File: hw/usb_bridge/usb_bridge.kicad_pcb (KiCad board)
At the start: 2 copper layers, 51 x 31 mm, 55 parts, among them J1 USB_C_Receptacle_USB2.0_14P, J2 DE9, J3 SWD, J4 BOOT, U1 CH340E, U2 MAX485E, U3 CH334R, U4 74LVC2G04, U5 MCP1754S-3302xCB, U6 TJA1051T-3, U7 STM32G0B1CBT, Y1 HCI XC53G2-12.000-F20LJDT, Y2 HCI XC53G2-8.000-F12NJHP

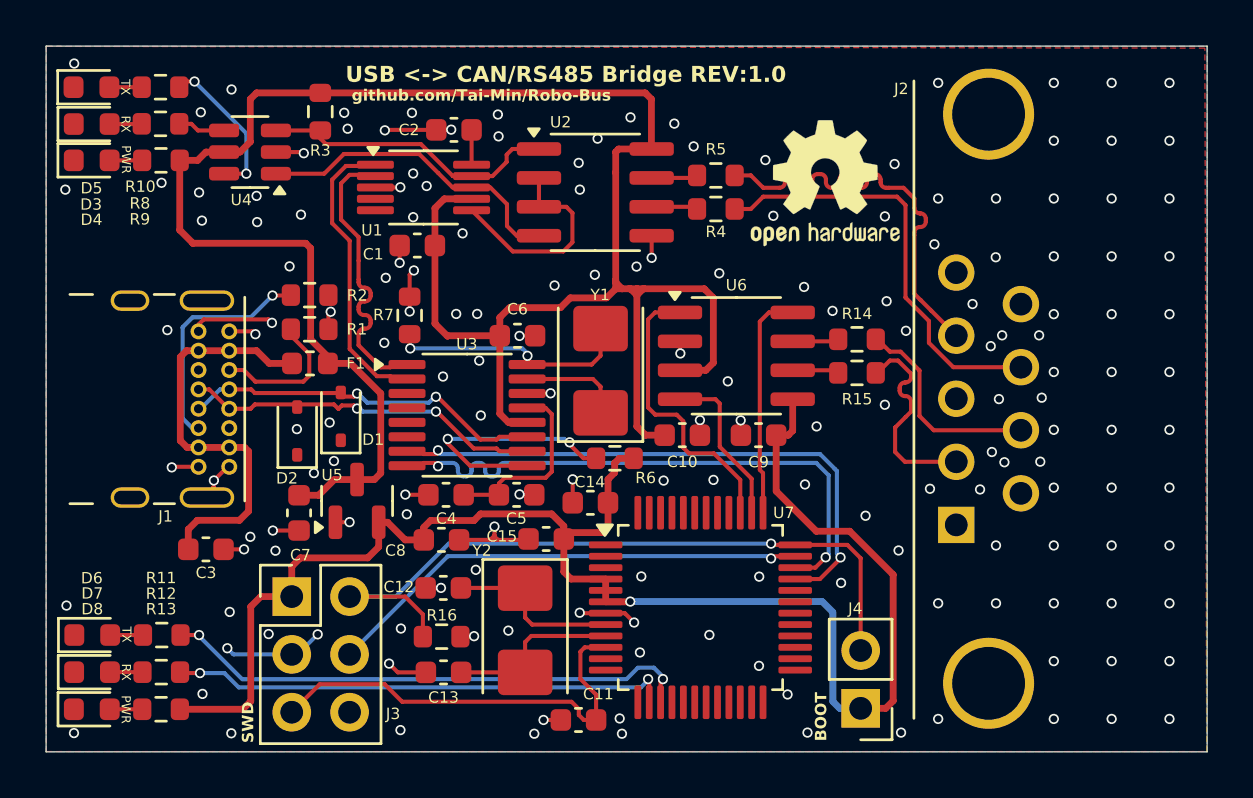
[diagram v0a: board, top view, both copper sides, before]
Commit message: Add jumpers and test points, add QR code
Signed-off-by: Mateusz Pająk <22417805+Tai-Min@users.noreply.github.com>
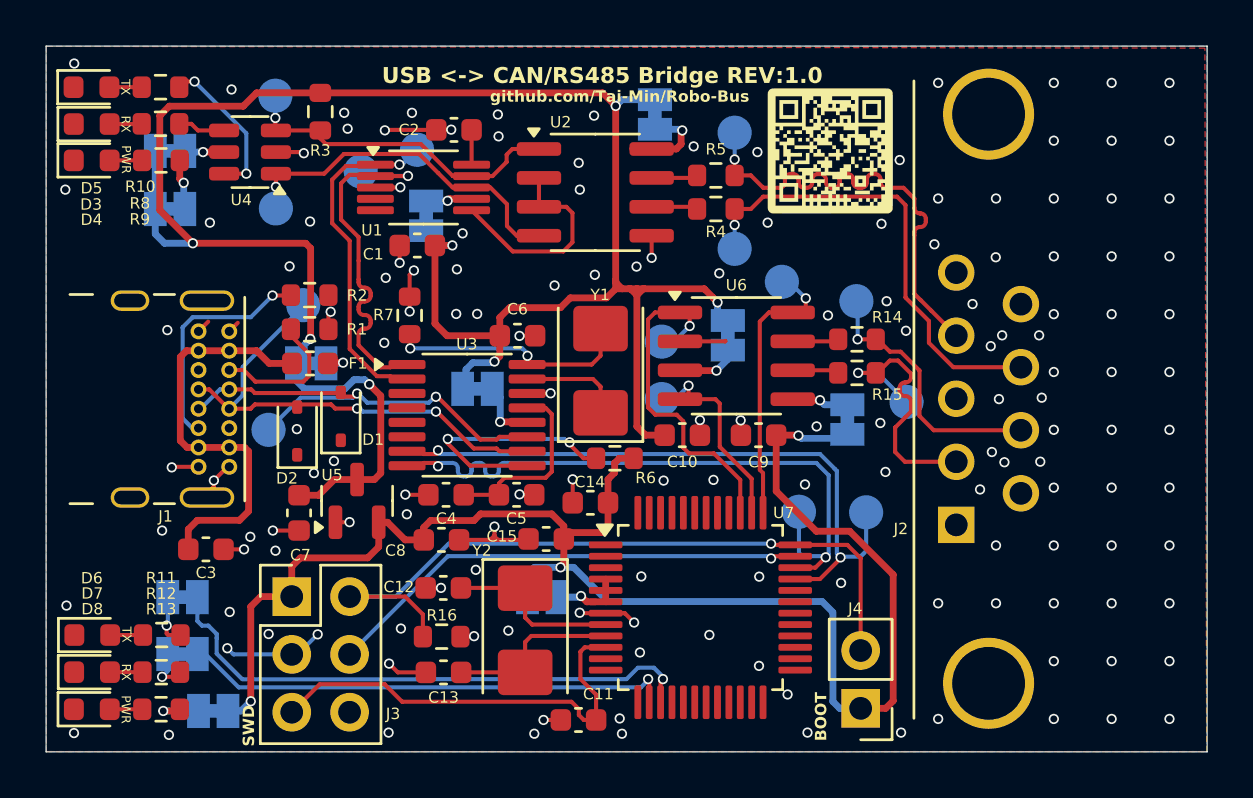
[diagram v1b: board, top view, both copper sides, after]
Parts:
- added G***: LOGO, symbols:robo-bus-qr-small, F.Cu at (160.9, 91.7)
- added JP1: Diode cutoff, Jumper:SolderJumper-2_P1.3mm_Bridged_Pad1.0x1.5mm, B.Cu at (131.9, 93.7)
- added JP10: Diode cutoff, Jumper:SolderJumper-2_P1.3mm_Bridged_Pad1.0x1.5mm, B.Cu at (132.4, 110.8)
- added JP11: Amp TP, Jumper:SolderJumper-2_P1.3mm_Bridged_Pad1.0x1.5mm, B.Cu at (148.2, 110.8)
- added JP12: Amp TP, Jumper:SolderJumper-2_P1.3mm_Bridged_Pad1.0x1.5mm, B.Cu at (161.7, 103.0)
- added JP2: Diode cutoff, Jumper:SolderJumper-2_P1.3mm_Bridged_Pad1.0x1.5mm, B.Cu at (133.8, 115.8)
- added JP3: Diode cutoff, Jumper:SolderJumper-2_P1.3mm_Bridged_Pad1.0x1.5mm, B.Cu at (131.9, 91.2)
- added JP4: Amp TP, Jumper:SolderJumper-2_P1.3mm_Bridged_Pad1.0x1.5mm, B.Cu at (138.1, 100.5)
- added JP5: Amp TP, Jumper:SolderJumper-2_P1.3mm_Bridged_Pad1.0x1.5mm, B.Cu at (145.4, 101.6)
- added JP6: Amp TP, Jumper:SolderJumper-2_P1.3mm_Bridged_Pad1.0x1.5mm, B.Cu at (156.4, 99.2)
- added JP7: Amp TP, Jumper:SolderJumper-2_P1.3mm_Bridged_Pad1.0x1.5mm, B.Cu at (153.2, 89.5)
- added JP8: Amp TP, Jumper:SolderJumper-2_P1.3mm_Bridged_Pad1.0x1.5mm, B.Cu at (143.2, 94.0)
- added JP9: Diode cutoff, Jumper:SolderJumper-2_P1.3mm_Bridged_Pad1.0x1.5mm, B.Cu at (132.4, 113.2)
- added TP1: TestPoint, TestPoint:TestPoint_Pad_D1.5mm, B.Cu at (158.8, 96.9)
- added TP10: TestPoint, TestPoint:TestPoint_Pad_D1.5mm, B.Cu at (137.8, 97.9)
- added TP11: TestPoint, TestPoint:TestPoint_Pad_D1.5mm, B.Cu at (136.2, 103.4)
- added TP12: TestPoint, TestPoint:TestPoint_Pad_D1.5mm, B.Cu at (156.7, 95.5)
- added TP13: TestPoint, TestPoint:TestPoint_Pad_D1.5mm, B.Cu at (156.7, 90.3)
- added TP14: TestPoint, TestPoint:TestPoint_Pad_D1.5mm, B.Cu at (164.2, 102.2)
- added TP15: TestPoint, TestPoint:TestPoint_Pad_D1.5mm, B.Cu at (162.1, 97.8)
- added TP2: TestPoint, TestPoint:TestPoint_Pad_D1.5mm, B.Cu at (153.5, 102.0)
- added TP3: TestPoint, TestPoint:TestPoint_Pad_D1.5mm, B.Cu at (153.5, 99.5)
- added TP4: TestPoint, TestPoint:TestPoint_Pad_D1.5mm, B.Cu at (136.6, 93.7)
- added TP5: TestPoint, TestPoint:TestPoint_Pad_D1.5mm, B.Cu at (136.5, 88.7)
- added TP6: TestPoint, TestPoint:TestPoint_Pad_D1.5mm, B.Cu at (140.3, 92.0)
- added TP7: TestPoint, TestPoint:TestPoint_Pad_D1.5mm, B.Cu at (142.8, 91.1)
- added TP8: TestPoint, TestPoint:TestPoint_Pad_D1.5mm, B.Cu at (162.5, 107.0)
- added TP9: TestPoint, TestPoint:TestPoint_Pad_D1.5mm, B.Cu at (159.5, 107.0)
- REF**: moved to B.Cu
- moved REF** 43.8 mm to (172.9, 110.4), turned to -90 degrees
- moved REF** 15.2 mm to (173.8, 100.4), turned to -90 degrees
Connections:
- F1 pad 2: +5V -> Net-(JP4-A)
- R10 pad 2: +5V -> Net-(JP1-A)
- R11 pad 2: /mcu/LED_TX -> Net-(JP10-A)
- R12 pad 2: /mcu/LED_RX -> Net-(JP9-A)
- R13 pad 2: +3.3V -> Net-(JP2-A)
- U1 pad 7: +5V -> Net-(JP8-A)
- U2 pad 8: +5V -> Net-(JP7-A)
- U3 pad 12: +5V -> Net-(JP5-A)
- U4 pad 5: +5V -> Net-(JP3-A)
- U6 pad 3: +5V -> Net-(JP6-A)
- U6 pad 5: +3.3V -> Net-(JP12-A)
- U7 pad 4: +3.3V -> Net-(JP11-A)
- U7 pad 5: +3.3V -> Net-(JP11-A)
- U7 pad 6: +3.3V -> Net-(JP11-A)
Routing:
- net /D-: track 15.9 -> 21.7 mm
- net /D+: track 16.1 -> 20.6 mm
- net Net-(JP7-A): track 0.00 -> 4.07 mm, vias 0 -> 1
- net /D_RS-: track 12.9 -> 16.5 mm, vias 0 -> 1
- net /CAN-: track 9.16 -> 12.6 mm, vias 0 -> 1
- net /D_CAN+: track 25.5 -> 28.6 mm
- net /D_CAN-: track 25.6 -> 28.5 mm
- net Net-(JP11-A): track 0.00 -> 2.81 mm, vias 0 -> 1
- net Net-(JP5-A): track 0.00 -> 2.79 mm, vias 0 -> 1
- net Net-(JP6-A): track 0.00 -> 2.71 mm, vias 0 -> 1
- net Net-(JP12-A): track 0.00 -> 2.50 mm, vias 0 -> 1
- net /CAN+: track 9.20 -> 11.7 mm, vias 0 -> 1
- net /mcu/CAN_TX: track 12.9 -> 15.4 mm, vias 0 -> 1
- net /mcu/CAN_S: track 10.1 -> 12.5 mm, vias 0 -> 1
- net /mcu/CAN_RX: track 7.20 -> 9.52 mm, vias 0 -> 1
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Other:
- board text added: "3V3 LED"
- board text added: "5V LED"
- board text added: "CAN AMP TP"
- board text added: "CAN IO AMP TP"
- board text added: "CAN RX"
- board text added: "CAN RX LED"
- board text added: "CAN S"
- board text added: "CAN TX"
- board text added: "CAN TX LED"
- board text added: "CAN+"
- board text added: "CAN-"
- board text added: "D+"
- board text added: "D+ CAN"
- board text added: "D+ RS485"
- board text added: "D-"
- board text added: "D- CAN"
- board text added: "D- RS485"
- board text added: "HUB AMP TP"
- board text added: "PWR AMP TP"
- board text added: "RS485 AMP TP"
- board text added: "RS485 LEDS"
- board text added: "RS485 RX"
- board text added: "RS485 TX"
- board text added: "RS485+"
- board text added: "RS485-"
- board text added: "STM AMP TP"
- board text added: "UART AMP TP"

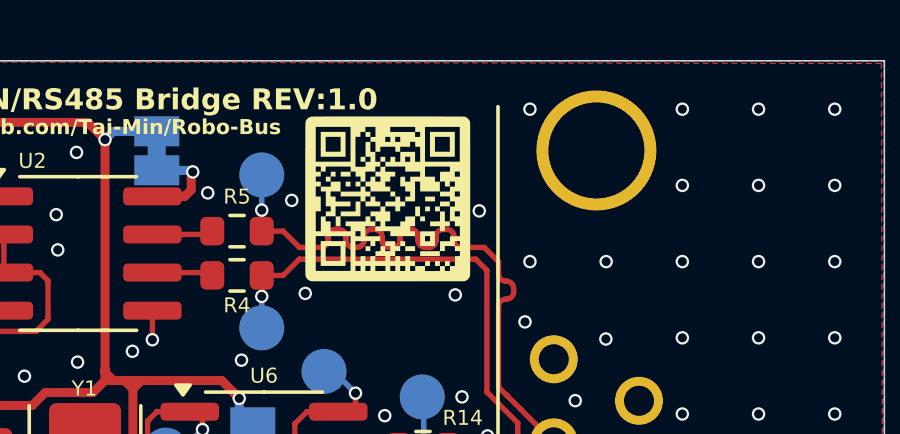
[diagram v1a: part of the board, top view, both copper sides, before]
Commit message: Add gnd test point
Signed-off-by: Mateusz Pająk <22417805+Tai-Min@users.noreply.github.com>
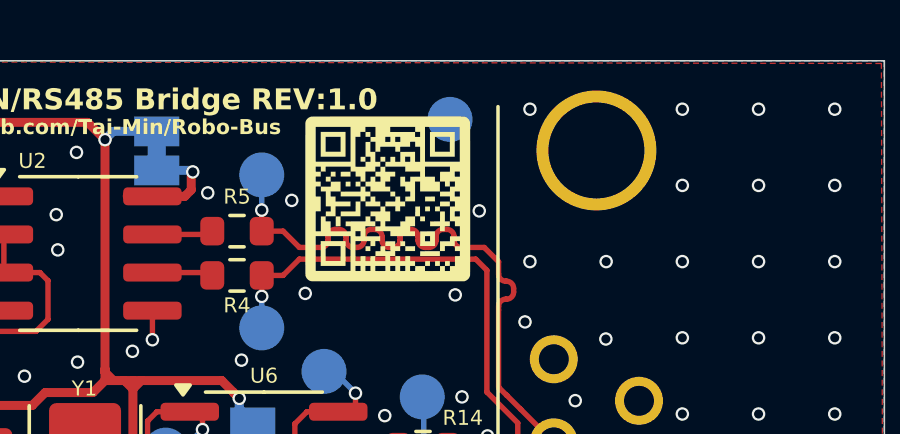
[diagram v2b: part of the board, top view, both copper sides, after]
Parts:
- added TP16: TestPoint, TestPoint:TestPoint_Pad_D1.5mm, B.Cu at (163.0, 88.5)
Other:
- board text added: "GND"
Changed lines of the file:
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@@
+	(footprint "TestPoint:TestPoint_Pad_D1.5mm"
+		(layer "B.Cu")
+		(at 162.975 88.5 180)
+		(descr "SMD pad as test Point, diameter 1.5mm")
+		(tags "test point SMD pad")
+		(property "Reference" "TP16"
+			(at 0 1.648 0)
+			(layer "B.SilkS")
+			(hide yes)
+			(effects
+				(font
+					(size 1 1)
+					(thickness 0.15)
+				)
+				(justify mirror)
+			)
+		)
+		(property "Value" "TestPoint"
+			(at 0 -1.75 0)
+			(layer "B.Fab")
+			(effects
+				(font
+					(size 1 1)
+					(thickness 0.15)
+				)
+				(justify mirror)
+			)
+		)
+		(property "Datasheet" "~"
+			(at 0 0 0)
+			(unlocked yes)
+			(layer "B.Fab")
+			(hide yes)
+			(effects
+				(font
+					(size 1.27 1.27)
+					(thickness 0.15)
+				)
+				(justify mirror)
+			)
+		)
+		(property "Description" "test point"
+			(at 0 0 0)
+			(unlocked yes)
+			(layer "B.Fab")
+			(hide yes)
+			(effects
+				(font
+					(size 1.27 1.27)
+					(thickness 0.15)
+				)
+				(justify mirror)
+			)
+		)
+		(property ki_fp_filters "Pin* Test*")
+		(sheetname "/")
+		(sheetfile "usb_bridge.kicad_sch")
+		(attr exclude_from_pos_files)
+		(fp_circle
+			(center 0 0)
+			(end 0 -0.95)
+			(stroke
+				(width 0.12)
+				(type solid)
+			)
+			(fill no)
+			(layer "B.SilkS")
+		)
+		(fp_circle
+			(center 0 0)
+			(end 1.25 0)
+			(stroke
+				(width 0.05)
+				(type solid)
+			)
+			(fill no)
+			(layer "B.CrtYd")
+		)
+		(fp_text user "${REFERENCE}"
+			(at 0 1.65 0)
+			(layer "B.Fab")
+			(effects
+				(font
+					(size 1 1)
+					(thickness 0.15)
+				)
+				(justify mirror)
+			)
+		)
+		(pad "1" smd circle
+			(at 0 0 180)
+			(size 1.5 1.5)
+			(layers "B.Cu" "B.Mask")
+			(net 1 "GND")
+			(pinfunction "1")
+			(pintype "passive")
+		)
+		(embedded_fonts no)
+	)
 	(footprint "TestPoint:TestPoint_Pad_D1.5mm"
 		(layer "B.Cu")
@@
 		(layer "B.SilkS")
 		(effects
+			(font
+				(size 0.5 0.5)
+				(thickness 0.125)
+				(bold yes)
+			)
+			(justify left bottom mirror)
+		)
+	)
+	(gr_text "GND"
+		(at 163.8 90.325 0)
+		(layer "B.SilkS")
+		(effects

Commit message: Change versioning
Signed-off-by: Mateusz Pająk <22417805+Tai-Min@users.noreply.github.com>
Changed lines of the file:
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@@
 	(paper "A4")
 	(title_block
-		(title "USB <-> CAN/RS485 Bridge")
+		(title "${TITLE}")
 		(date "2025-11-24")
-		(rev "1.0")
+		(rev "${REVISION}")
 	)
 	(layers
@@
 		)
 	)
-	(property "REVISION" "1.0")
+	(property "REVISION" "1.0.0d")
 	(property "TITLE" "USB <-> CAN / RS485 ADAPTER")
 	(net 0 "")
@@
 	)
 	(gr_text "${TITLE} REV:${REVISION}"
-		(at 141.2 88.25 0)
+		(at 163.7792 88.2904 0)
 		(layer "F.SilkS")
 		(effects
@@
 				(bold yes)
 			)
-			(justify left bottom)
+			(justify right bottom)
 		)
 	)

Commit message: Cleanup
Signed-off-by: Mateusz Pająk <22417805+Tai-Min@users.noreply.github.com>
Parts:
- removed JP1, JP10, JP2, JP3, JP9: Diode cutoff, Jumper:SolderJumper-2_P1.3mm_Bridged_Pad1.0x1.5mm
- removed JP11, JP12, JP4, JP5, JP6, JP7, JP8: Amp TP, Jumper:SolderJumper-2_P1.3mm_Bridged_Pad1.0x1.5mm
- removed the R13 at (131.5, 115.7)
- removed the TP10 at (137.8, 97.9)
- removed the TP11 at (136.2, 103.4)
- added D9: SM712-02HTG, Package_TO_SOT_SMD:SOT-23, F.Cu at (161.8, 95.8)
- D8: value green -> CDSOT23-T24CAN; footprint LED_SMD:LED_0603_1608Metric -> Package_TO_SOT_SMD:SOT-23
- moved TP1 35.7 mm to (129.9, 102.0)
- moved D8 35.3 mm to (161.8, 104.1), turned to 180 degrees
- moved D6 19.3 mm to (128.5, 93.2)
- moved R11 19.3 mm to (131.5, 93.2)
- moved D7 19.3 mm to (128.5, 94.8)
- moved R12 19.3 mm to (131.5, 94.8)
- moved TP13 5.78 mm to (159.3, 102.1)
- moved TP14 5.78 mm to (159.3, 99.5)
- moved TP8 4.46 mm to (159.6, 110.4)
- moved TP6 3.05 mm to (142.9, 93.5)
- moved TP15 1.90 mm to (163.6, 98.9)
- moved TP10 1.66 mm to (137.2, 92.1)
- moved TP5 1.34 mm to (156.7, 91.7)
- moved TP4 1.21 mm to (156.7, 94.2)
- moved TP11 1.12 mm to (137.2, 89.6)
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- renumbered C14 to C13, C13 to C14, C3 to C2, C2 to C3, C6 to C5, C5 to C6, D5 to D1, D1 to D2, D2 to D3, D3 to D4, D4 to D5, R10 to R1, R9 to R10, R14 to R13, R15 to R14, R16 to R15, R1 to R2, R2 to R3, R3 to R4, R6 to R5, R7 to R6, R4 to R7, R5 to R8, R8 to R9, TP16 to TP1, TP4 to TP10, TP5 to TP11, TP1 to TP12, TP2 to TP13, TP3 to TP14, TP14 to TP16, TP12 to TP4, TP13 to TP5
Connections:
- net /RX renamed /RS_RX
- net /TX renamed /RS_TX
- D8 pad 1: GND -> /CAN-
- D8 pad 2: Net-(D8-A) -> /CAN+
- F1 pad 2: Net-(JP4-A) -> +5V
- R1 pad 2: Net-(JP1-A) -> +5V
- R11 pad 2: Net-(JP10-A) -> /mcu/LED_TX
- R12 pad 2: Net-(JP9-A) -> /mcu/LED_RX
- U1 pad 7: Net-(JP8-A) -> +5V
- U2 pad 8: Net-(JP7-A) -> +5V
- U3 pad 12: Net-(JP5-A) -> +5V
- U4 pad 5: Net-(JP3-A) -> +5V
- U6 pad 3: Net-(JP6-A) -> +5V
- U6 pad 5: Net-(JP12-A) -> +3.3V
- U7 pad 4: Net-(JP11-A) -> +3.3V
- U7 pad 5: Net-(JP11-A) -> +3.3V
- U7 pad 6: Net-(JP11-A) -> +3.3V
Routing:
- net /mcu/LED_RX: track 21.6 -> 41.7 mm, vias 1 -> 2
- net /mcu/LED_TX: track 24.6 -> 43.6 mm, vias 1 -> 2
- net GND: track 40.3 -> 28.1 mm, vias 152 -> 176
- net +3.3V: track 71.3 -> 60.1 mm, vias 3 -> 0
- net /D-: track 21.7 -> 15.9 mm
- net /D+: track 20.6 -> 16.2 mm
- net Net-(JP7-A): track 4.07 -> 0.00 mm, vias 1 -> 0
- net /mcu/CAN_RX: track 9.52 -> 13.4 mm
- net /mcu/CAN_TX: track 15.4 -> 19.2 mm
- net /CAN+: track 11.7 -> 14.8 mm
- net Net-(JP11-A): track 2.81 -> 0.00 mm, vias 1 -> 0
- net Net-(JP5-A): track 2.79 -> 0.00 mm, vias 1 -> 0
- net Net-(JP6-A): track 2.71 -> 0.00 mm, vias 1 -> 0
- net Net-(JP12-A): track 2.50 -> 0.00 mm, vias 1 -> 0
- net /D_CAN+: track 28.6 -> 26.2 mm
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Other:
- board text added: "+"
- board text added: "-"
- board text added: "CAN"
- board text added: "RS485"
- board text added: "S"
- board text removed: "3V3 LED"
- board text removed: "5V LED"
- board text removed: "CAN AMP TP"
- board text removed: "CAN IO AMP TP"
- board text removed: "CAN RX"
- board text removed: "CAN RX LED"
- board text removed: "CAN S"
- board text removed: "CAN TX"
- board text removed: "CAN TX LED"
- board text removed: "CAN+"
- board text removed: "CAN-"
- board text removed: "D+ CAN"
- board text removed: "D+ RS485"
- board text removed: "D- CAN"
- board text removed: "D- RS485"
- board text removed: "HUB AMP TP"
- board text removed: "PWR AMP TP"
- board text removed: "RS485 AMP TP"
- board text removed: "RS485 LEDS"
- board text removed: "RS485 RX"
- board text removed: "RS485 TX"
- board text removed: "RS485+"
- board text removed: "RS485-"
- board text removed: "STM AMP TP"
- board text removed: "SWD"
- board text removed: "This documentation describes Open Hardware and is licensed under the CERN OHL v. 1.2. You may redistribute and modify this documentation under the terms of the CERN OHL v.1.2.(http://ohwr.org/cernohl). This documentation is distributed WITHOUT ANY EXPRESS OR IMPLIED WARRANTY, INCLUDING OF MERCHANTABILITY, SATISFACTORY QUALITY AND FITNESS FOR A PARTICULAR PURPOSE. Please see the CERN OHL v.1.2 for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"
- board text removed: "UART AMP TP"

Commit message: Fix parity issue
Signed-off-by: Mateusz Pająk <22417805+Tai-Min@users.noreply.github.com>
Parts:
- F1: value 500mA -> BSMD0603C-0500T
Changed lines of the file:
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@@
 			)
 		)
-		(property "Value" "500mA"
+		(property "Value" "BSMD0603C-0500T"
 			(at 0 1.43 0)
 			(layer "F.Fab")
@@
 			)
 		)
-		(property "Description" "BSMD0603C-0500T"
+		(property "Description" "500mA"
 			(at 0 0 0)
 			(layer "F.Fab")

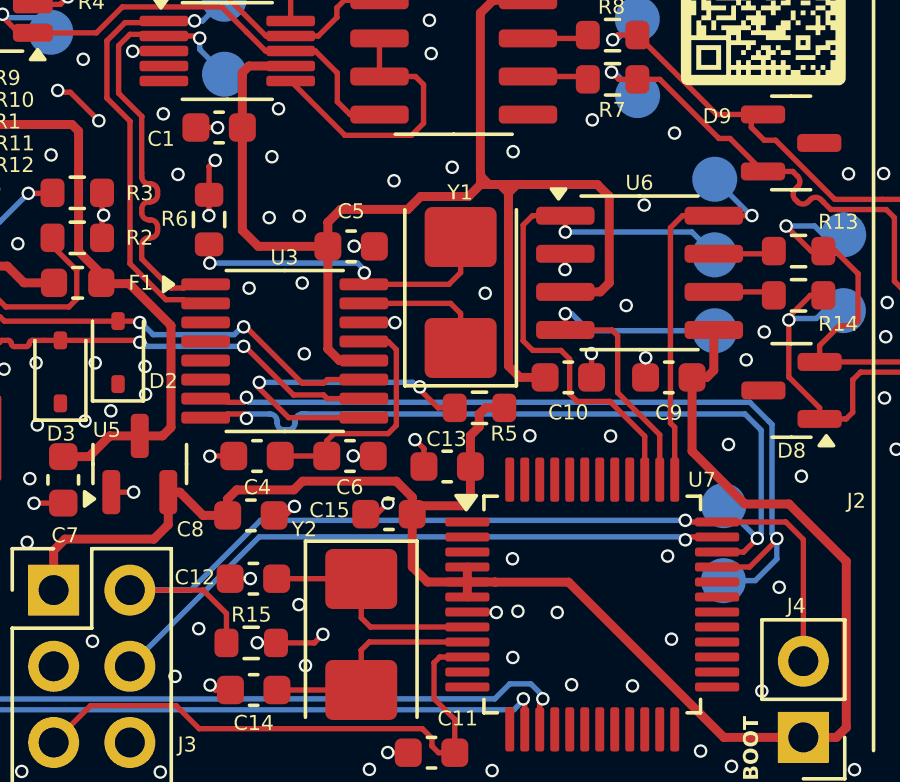
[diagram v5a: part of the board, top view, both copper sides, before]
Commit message: Minor PCB fixes
Signed-off-by: Mateusz Pająk <22417805+Tai-Min@users.noreply.github.com>
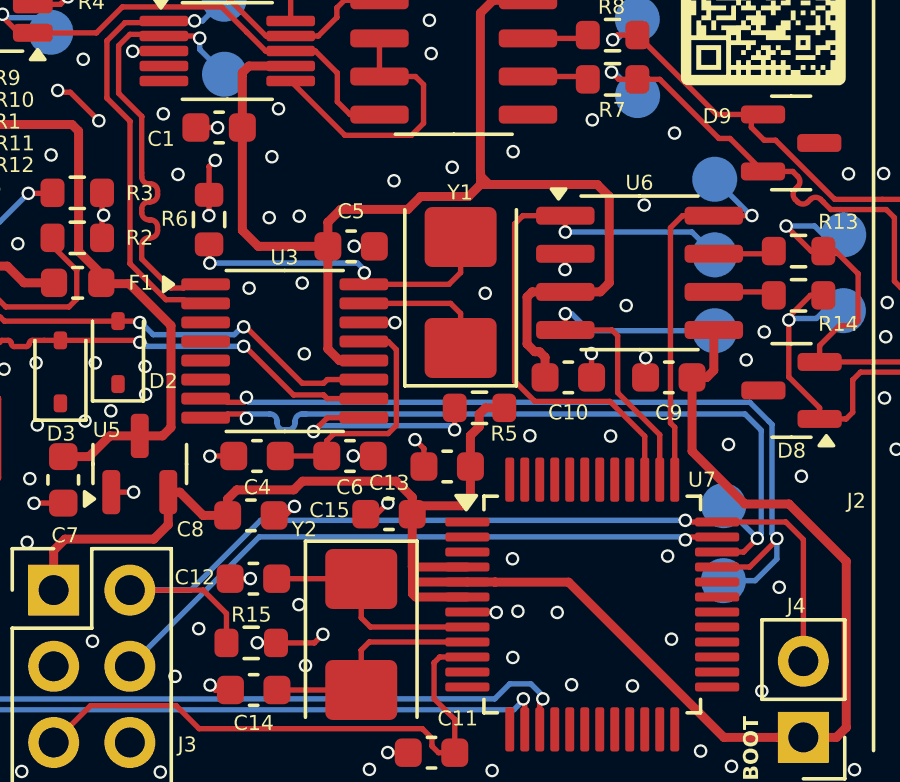
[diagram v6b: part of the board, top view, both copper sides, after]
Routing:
- net +5V: track 99.6 -> 95.8 mm
- net Net-(U3-~{RESET}/CDP): track 11.0 -> 7.44 mm
- net +3.3V: track 60.1 -> 63.5 mm
- net /mcu/CAN_TX: track 19.2 -> 19.9 mm
